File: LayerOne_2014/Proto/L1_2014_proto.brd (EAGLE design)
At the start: 99 x 48.8 mm, 87 parts, among them IC10 74XX244-OCTAL-TRISTATE-BUFFERS, IC11 CD4066, IC202 ADC08060, IC3 PQ1X331M2ZP-3V3-LDO-SOT-23-5, IC4 HCU-INVERTER, IC6 MCP6294, IC9 74XX244-OCTAL-TRISTATE-BUFFERS, U1 XC3S50AVQ100, U201 FB

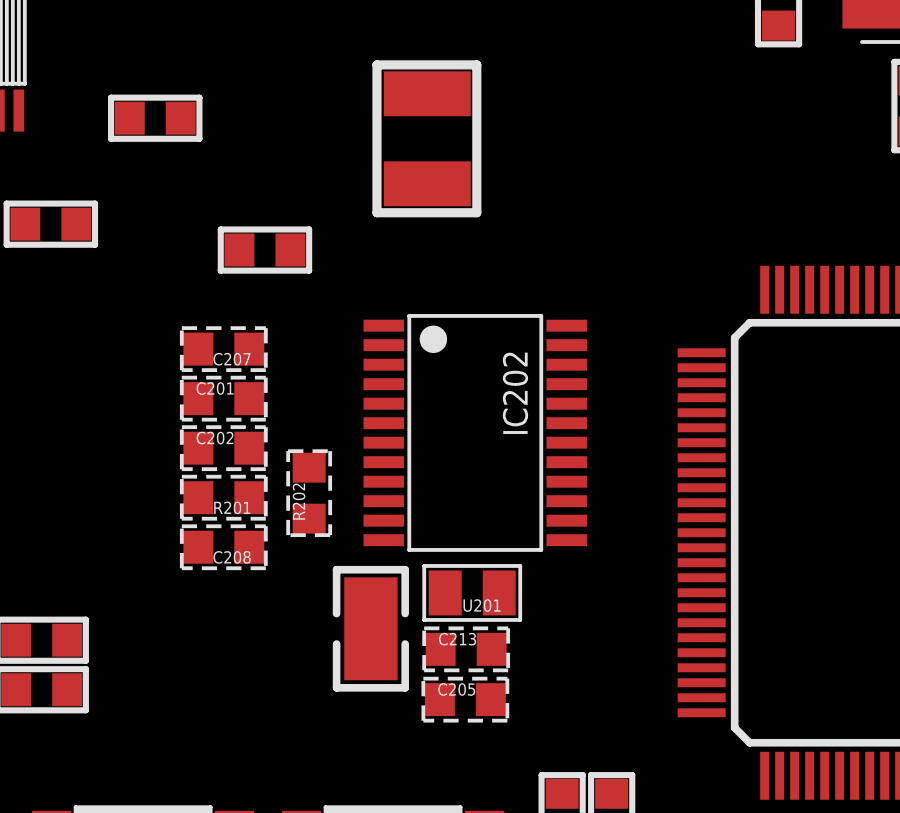
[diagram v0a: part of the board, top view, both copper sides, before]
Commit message: 
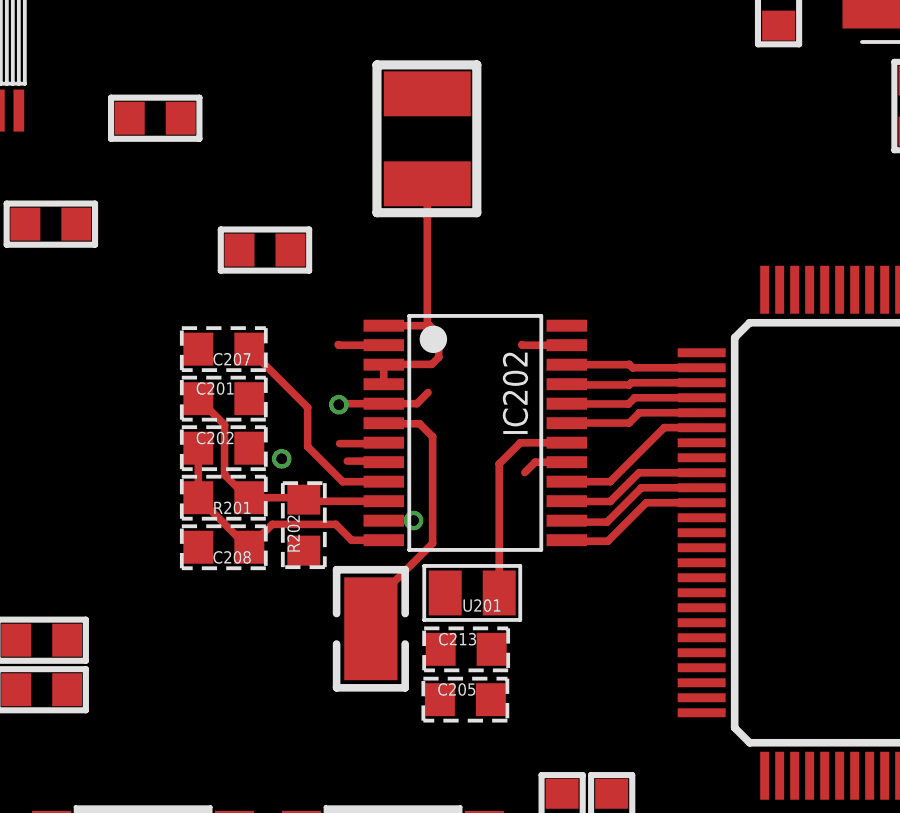
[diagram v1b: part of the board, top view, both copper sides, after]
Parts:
- moved R202 1.08 mm to (30.5, 16.3)
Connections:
- removed net 13.56MHZ_CLK: C3.1, R1.2, R2.2, XT1.B
- net 1356_CRYSTAL: now also C3.1, R1.2, R2.2, XT1.B
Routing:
- net +3V3: track 0.00 -> 19.7 mm
- net GND: track 0.00 -> 11.3 mm, vias 0 -> 3
- net ADC_IN: track 0.00 -> 9.07 mm
- net N$23: track 0.00 -> 8.57 mm
- net N$26: track 0.00 -> 7.08 mm
- net VADC: track 0.00 -> 6.85 mm
- net ADC5: track 0.00 -> 5.25 mm
- net ADC8: track 0.00 -> 5.04 mm
- net ADC7: track 0.00 -> 4.99 mm
- net ADC6: track 0.00 -> 4.90 mm
- net ADC4: track 0.00 -> 4.64 mm
- net ADC3: track 0.00 -> 4.59 mm
- net ADC1: track 0.00 -> 4.55 mm
- net ADC2: track 0.00 -> 4.54 mm

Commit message: 
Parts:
- added U2: STM32-M-64-LQFP, stm32:LQFP64
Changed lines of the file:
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@@
 <layer number="223" name="223bmp" color="24" fill="1" visible="no" active="no"/>
 <layer number="224" name="224bmp" color="25" fill="1" visible="no" active="no"/>
+<layer number="231" name="Eagle3D_PG1" color="14" fill="1" visible="yes" active="yes"/>
+<layer number="232" name="Eagle3D_PG2" color="14" fill="2" visible="yes" active="yes"/>
+<layer number="233" name="Eagle3D_PG3" color="14" fill="4" visible="yes" active="yes"/>
 <layer number="250" name="Descript" color="7" fill="1" visible="no" active="yes"/>
 <layer number="251" name="SMDround" color="7" fill="1" visible="no" active="yes"/>
@@
 <element name="C1" library="  merged" package="RLC_0603" value="100n" x="29.1592" y="25.4508" rot="R180"/>
 <element name="U1" library="xilinx_devices" package="VQ100" value="XC3S50AVQ100" x="51.816" y="16.0274" rot="R270"/>
+<element name="U2" library="stm32" package="LQFP64" value="STM32-M-64-LQFP" x="77.7748" y="21.0312"/>
 </elements>
 <signals>

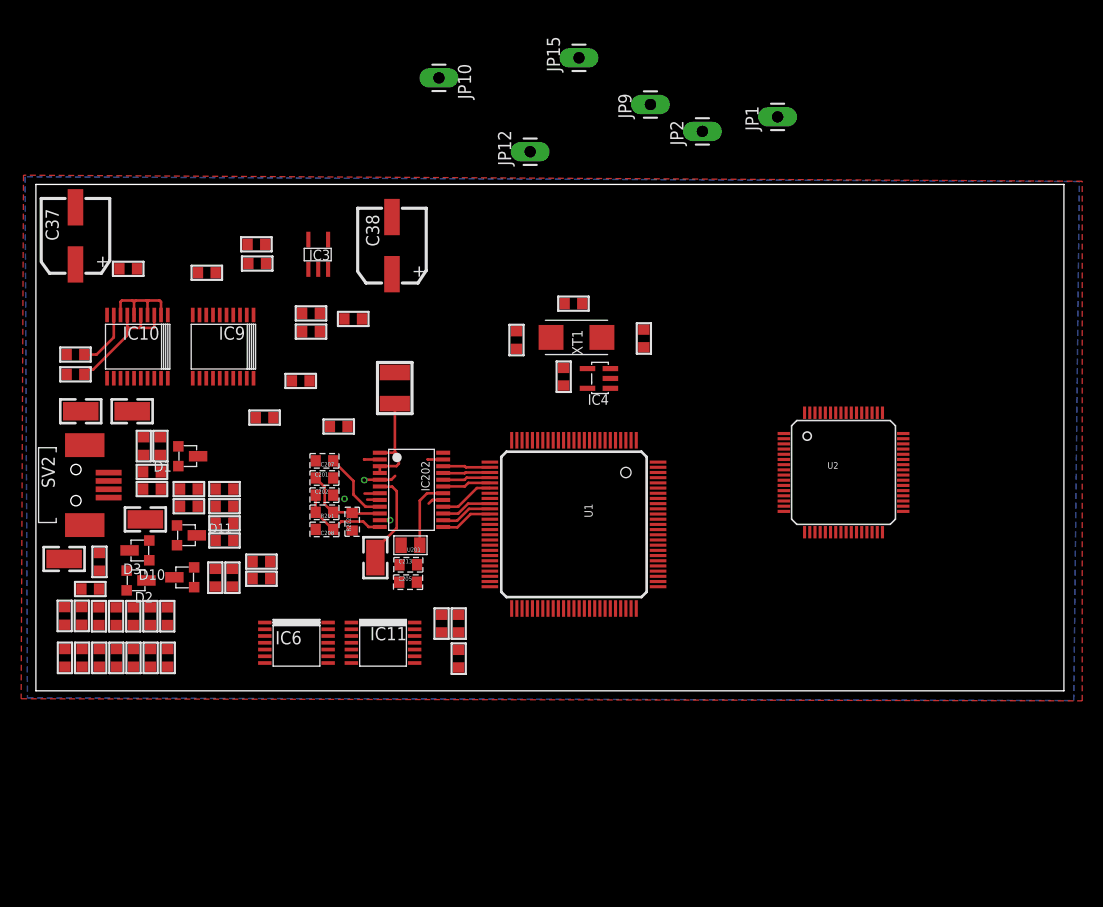
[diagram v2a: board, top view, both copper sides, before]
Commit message: 
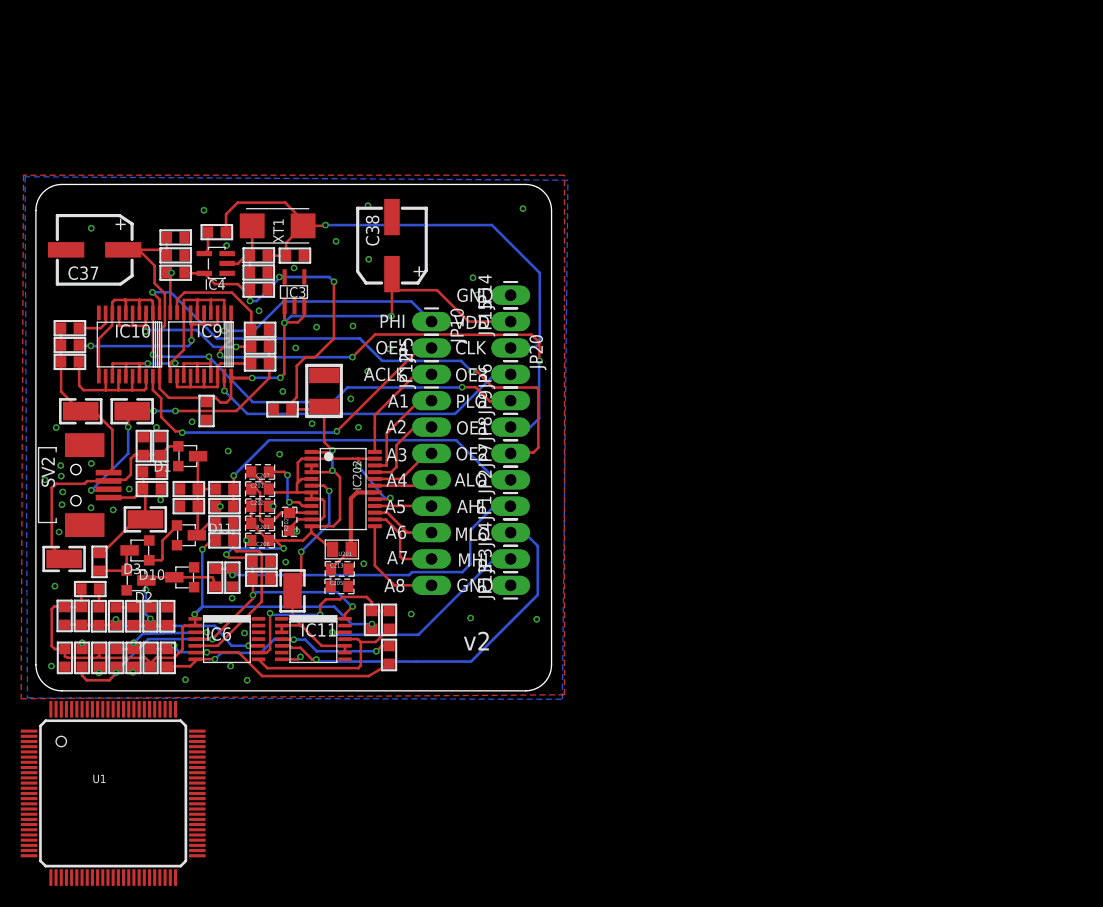
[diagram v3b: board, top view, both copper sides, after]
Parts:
- removed U2: STM32-M-64-LQFP, stm32:LQFP64
- added JP11: (no value), SparkFun:1X08_LONGPADS
- added JP13, JP14, JP20, JP3, JP4, JP5, JP6, JP7, JP8: M01PTH_LONGPAD, SparkFun:1X01_LONGPAD
- moved U1 51.4 mm to (7.44, -9.88), turned to 0 degrees
- moved JP1 45.5 mm to (45.7, 17.8)
- moved IC4 38.5 mm to (18.4, 40.2)
- moved JP2 38.3 mm to (45.7, 20.3)
- moved C2 37.6 mm to (21.5, 40.3), turned to 0 degrees
- moved R2 36.2 mm to (17.4, 44.2), turned to 0 degrees
- moved JP9 31.5 mm to (45.7, 27.9)
- moved XT1 30.7 mm to (21.0, 44.8)
- moved R1 30.7 mm to (21.5, 41.9)
- moved JP15 26.2 mm to (45.7, 35.6)
- moved JP10 23.5 mm to (38.1, 35.6)
- moved JP12 23.4 mm to (38.1, 30.5)
- moved C3 22.8 mm to (24.9, 41.9), turned to 0 degrees
- moved R22 22.5 mm to (3.28, 33.3)
- moved C23 19.3 mm to (13.5, 43.7), turned to 0 degrees
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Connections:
- new net 13.56MHZ_CLK: C3.1, JP20.1, R1.2, R2.2, XT1.B
- net 1356_CRYSTAL: no longer C3.1, R1.2, R2.2, XT1.B
- net ADC1: now also JP11.1
- net ADC2: now also JP11.2
- net ADC3: now also JP11.3
- net ADC4: now also JP11.4
- net ADC5: now also JP11.5
- net ADC6: now also JP11.6
- net ADC7: now also JP11.7
- net ADC8: now also JP11.8
- net GND: now also JP13.1, JP14.1
- net MUXSEL_HIPKD: now also JP3.1
- net MUXSEL_LOPKD: now also JP4.1
- net PWR_OE1: now also JP8.1
- net PWR_OE2: now also JP7.1
- net PWR_OE3: now also JP6.1
- net PWR_OE4: now also JP5.1
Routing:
- net +3V3: track 19.7 -> 115.6 mm, vias 0 -> 11
- net VDD: track 0.00 -> 78.9 mm, vias 0 -> 4
- net PWR_LO: track 9.32 -> 65.2 mm, vias 0 -> 3
- net VMID: track 0.00 -> 54.9 mm, vias 0 -> 3
- net PWR_OE2: track 0.00 -> 51.8 mm, vias 0 -> 2
- net PWR_HI: track 0.00 -> 51.0 mm, vias 0 -> 3
- net 13.56MHZ_CLK: track 0.00 -> 50.7 mm, vias 0 -> 1
- net PWR_OE1: track 0.00 -> 47.0 mm, vias 0 -> 3
- net MUXSEL_LOPKD: track 0.00 -> 35.9 mm, vias 0 -> 1
- net PWR_OE4: track 0.00 -> 34.3 mm, vias 0 -> 2
- net AMPL_HI: track 0.00 -> 33.7 mm, vias 0 -> 1
- net AMPL_LO: track 0.00 -> 32.6 mm, vias 0 -> 1
- net GND: track 11.3 -> 43.5 mm, vias 3 -> 60
- net PWR_OE3: track 0.00 -> 31.5 mm, vias 0 -> 1
- net N$31: track 0.00 -> 30.6 mm, vias 0 -> 4
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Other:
- board size 99 x 48.8 mm -> 49.7 x 48.8 mm
- board text added: "A1"
- board text added: "A2"
- board text added: "A3"
- board text added: "A4"
- board text added: "A5"
- board text added: "A6"
- board text added: "A7"
- board text added: "A8"
- board text added: "ACLK"
- board text added: "AHI"
- board text added: "ALO"
- board text added: "CLK"
- board text added: "GND"
- board text added: "MHI"
- board text added: "MLO"
- board text added: "OE1"
- board text added: "OE2"
- board text added: "OE3"
- board text added: "OE4"
- board text added: "PHI"
- board text added: "PLO"
- board text added: "VDD"
- board text added: "v2"

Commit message: 
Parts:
- moved U1 75.4 mm to (77.8, 17.2), turned to 270 degrees
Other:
- board size 49.7 x 48.8 mm -> 92.8 x 48.8 mm
